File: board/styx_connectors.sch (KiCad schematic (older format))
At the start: 15 parts, among them J3 Conn_01x08, J4 Styx_P4, J5 Styx_P5

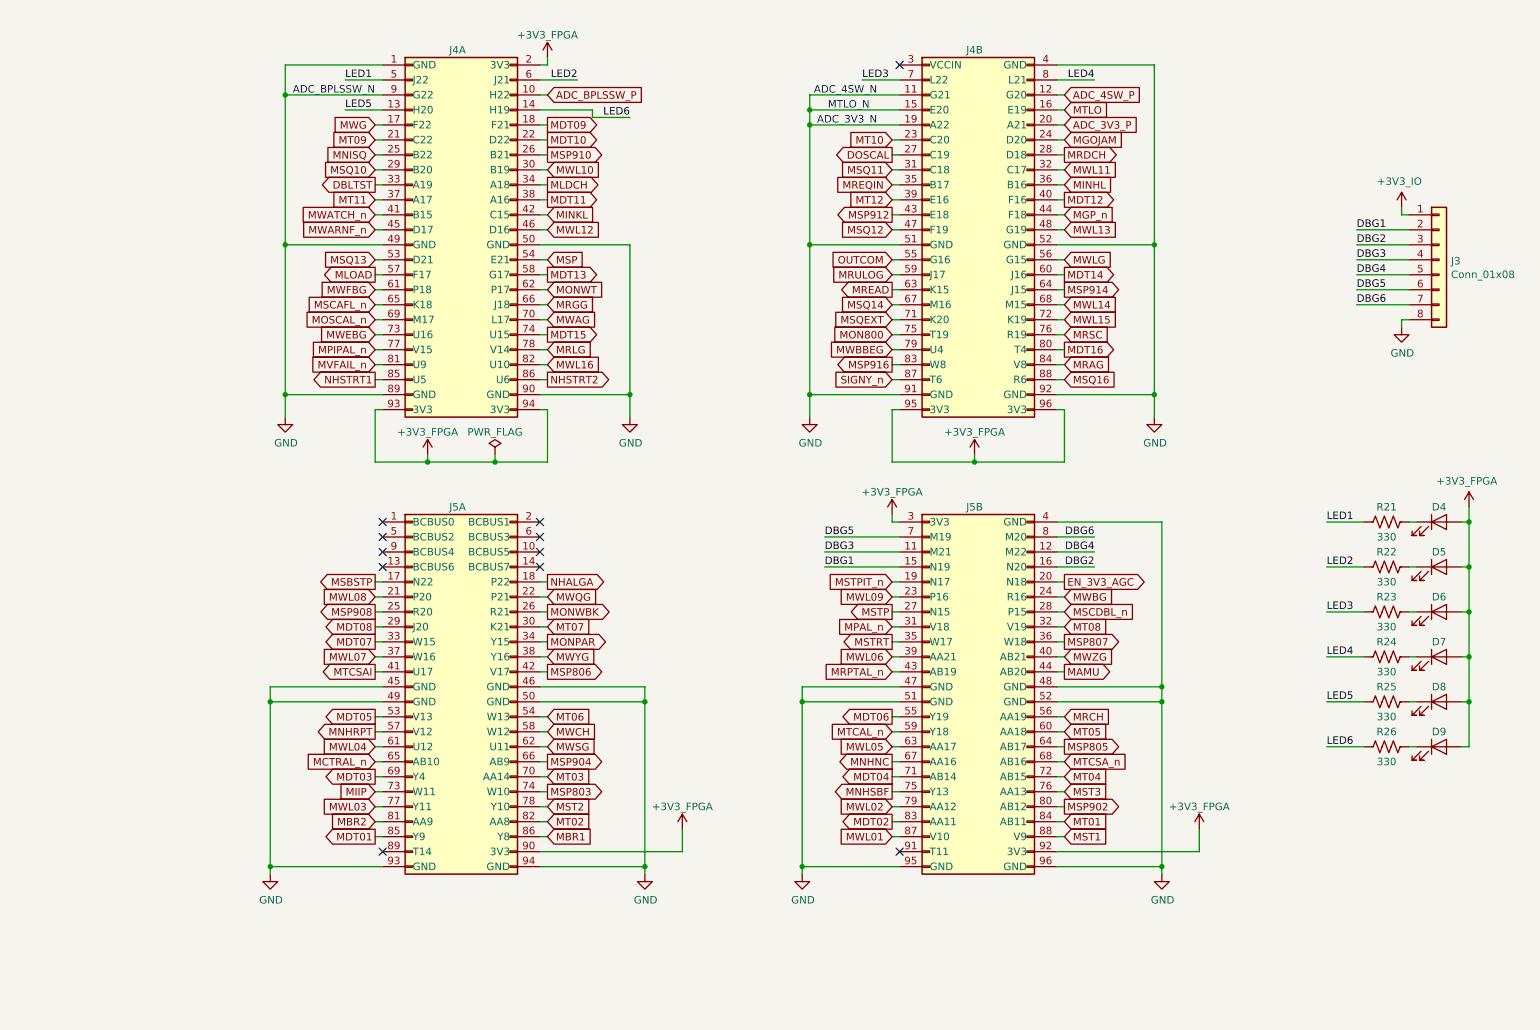
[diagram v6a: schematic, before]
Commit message: Redid the mechanical outline of the board; further development/layout
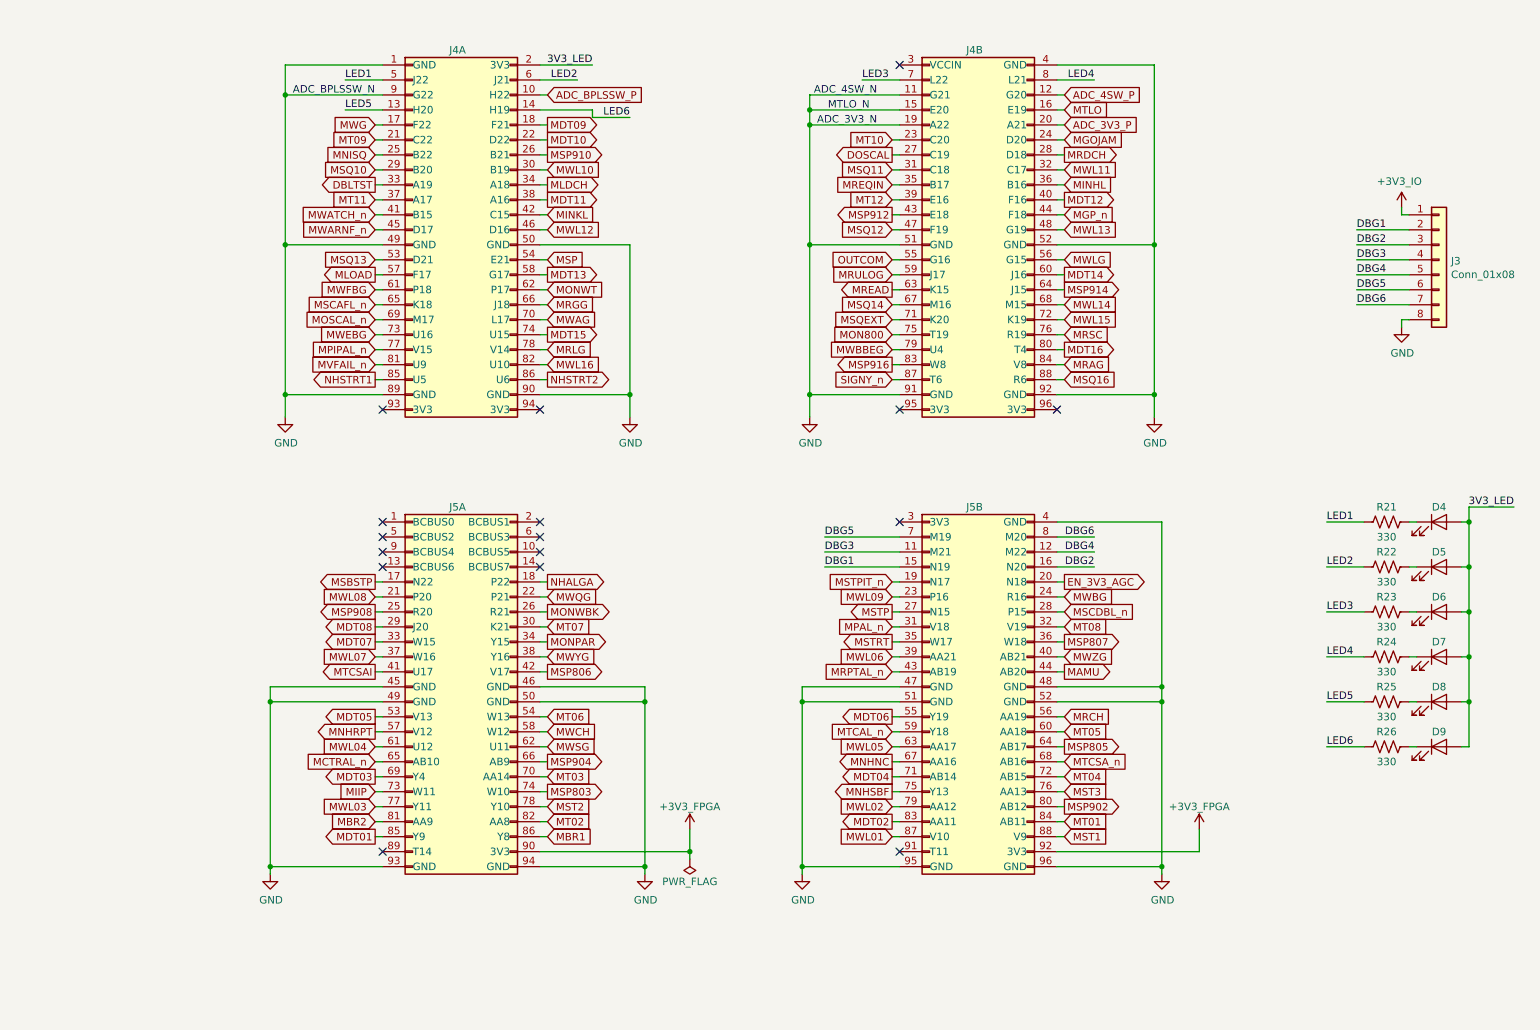
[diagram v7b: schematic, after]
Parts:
- J3: footprint Connector_PinHeader_2.54mm:PinHeader_2x04_P2.54mm_Vertical -> Connector_PinSocket_2.54mm:PinSocket_2x04_P2.54mm_Vertical
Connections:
- net +3V3_FPGA: no longer D4.2 (A), D5.2 (A), D6.2 (A), D7.2 (A), D8.2 (A), D9.2 (A), J4.2 (3V3), J4.93 (3V3), J4.94 (3V3), J4.95 (3V3), J4.96 (3V3), J5.3 (3V3)
- new net 3V3_LED: D4.2 (A), D5.2 (A), D6.2 (A), D7.2 (A), D8.2 (A), D9.2 (A), J4.2 (3V3)
- no-connect marks 11 -> 16
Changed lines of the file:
@@
 NoConn ~ 6150 850
 Wire Wire Line
-	3750 850  3800 850
-Wire Wire Line
-	3800 850  3800 800
-$Comp
-L agc_monitor:+3V3_FPGA #PWR0144
-U 1 1 5E187E74
-P 3800 800
-F 0 "#PWR0144" H 3800 650 50  0001 C CNN
-F 1 "+3V3_FPGA" H 3800 950 50  0000 C CNN
-F 2 "" H 3800 800 50  0001 C CNN
-F 3 "" H 3800 800 50  0001 C CNN
-	1    3800 800
-	1    0    0    -1
-$EndComp
+	3750 850  4100 850
 Text GLabel 2650 1450 0    50   Input ~ 0
 MNISQ
@@
 Wire Wire Line
 	3800 2450 3750 2450
-Wire Wire Line
-	2700 3150 2650 3150
-Wire Wire Line
-	2650 3150 2650 3500
-Wire Wire Line
-	2650 3500 3000 3500
-Wire Wire Line
-	3800 3500 3800 3150
-Wire Wire Line
-	3800 3150 3750 3150
-$Comp
-L agc_monitor:+3V3_FPGA #PWR0146
-U 1 1 5E198095
-P 3000 3450
-F 0 "#PWR0146" H 3000 3300 50  0001 C CNN
-F 1 "+3V3_FPGA" H 3000 3600 50  0000 C CNN
-F 2 "" H 3000 3450 50  0001 C CNN
-F 3 "" H 3000 3450 50  0001 C CNN
-	1    3000 3450
-	1    0    0    -1
-$EndComp
-Wire Wire Line
-	3000 3500 3000 3450
-Connection ~ 3000 3500
-Wire Wire Line
-	3000 3500 3450 3500
 Text GLabel 6100 1650 0    50   Input ~ 0
 MREQIN
@@
 	1    0    0    -1
 $EndComp
-Wire Wire Line
-	6100 3150 6100 3500
-Wire Wire Line
-	6100 3500 6650 3500
-Wire Wire Line
-	7250 3500 7250 3150
-$Comp
-L agc_monitor:+3V3_FPGA #PWR0148
-U 1 1 5E1A97CC
-P 6650 3450
-F 0 "#PWR0148" H 6650 3300 50  0001 C CNN
-F 1 "+3V3_FPGA" H 6650 3600 50  0000 C CNN
-F 2 "" H 6650 3450 50  0001 C CNN
-F 3 "" H 6650 3450 50  0001 C CNN
-	1    6650 3450
-	1    0    0    -1
-$EndComp
-Wire Wire Line
-	6650 3500 6650 3450
-Connection ~ 6650 3500
-Wire Wire Line
-	6650 3500 7250 3500
-Wire Wire Line
-	6150 3150 6100 3150
-Wire Wire Line
-	7250 3150 7200 3150
 Text Notes 6000 1050 2    50   ~ 0
 ADC_4SW_N
@@
 	2650 2950 2700 2950
 Wire Wire Line
-	3750 6100 4700 6100
-Wire Wire Line
-	4700 6100 4700 5950
+	3750 6100 4750 6100
+Wire Wire Line
+	4750 6100 4750 5950
 $Comp
 L agc_monitor:+3V3_FPGA #PWR0150
 U 1 1 5E3AF74D
-P 4700 5950
-F 0 "#PWR0150" H 4700 5800 50  0001 C CNN
-F 1 "+3V3_FPGA" H 4700 6100 50  0000 C CNN
-F 2 "" H 4700 5950 50  0001 C CNN
-F 3 "" H 4700 5950 50  0001 C CNN
-	1    4700 5950
+P 4750 5950
+F 0 "#PWR0150" H 4750 5800 50  0001 C CNN
+F 1 "+3V3_FPGA" H 4750 6100 50  0000 C CNN
+F 2 "" H 4750 5950 50  0001 C CNN
+F 3 "" H 4750 5950 50  0001 C CNN
+	1    4750 5950
 	1    0    0    -1
 $EndComp
@@
 	7900 6250 7900 6200
 Connection ~ 7900 6200
-Wire Wire Line
-	6150 3900 6100 3900
-Wire Wire Line
-	6100 3900 6100 3850
-$Comp
-L agc_monitor:+3V3_FPGA #PWR0155
-U 1 1 5E412C0B
-P 6100 3850
-F 0 "#PWR0155" H 6100 3700 50  0001 C CNN
-F 1 "+3V3_FPGA" H 6100 4000 50  0000 C CNN
-F 2 "" H 6100 3850 50  0001 C CNN
-F 3 "" H 6100 3850 50  0001 C CNN
-	1    6100 3850
-	1    0    0    -1
-$EndComp
 Text GLabel 6100 2650 0    50   Input ~ 0
 MON800
@@
 Wire Wire Line
 	9500 2550 9550 2550
-$Comp
-L agc_monitor:+3V3_IO #PWR0158
-U 1 1 5E993DA6
-P 9500 1800
-F 0 "#PWR0158" H 9500 1650 50  0001 C CNN
-F 1 "+3V3_IO" H 9485 1973 50  0000 C CNN
-F 2 "" H 9500 1800 50  0001 C CNN
-F 3 "" H 9500 1800 50  0001 C CNN
-	1    9500 1800
-	1    0    0    -1
-$EndComp
-Wire Wire Line
-	9500 1800 9500 1850
 Wire Wire Line
 	9500 1850 9550 1850
@@
 	9950 3900 9950 3800
 $Comp
-L agc_monitor:+3V3_FPGA #PWR0159
-U 1 1 5EA31B9C
-P 9950 3800
-F 0 "#PWR0159" H 9950 3650 50  0001 C CNN
-F 1 "+3V3_FPGA" H 9935 3973 50  0000 C CNN
-F 2 "" H 9950 3800 50  0001 C CNN
-F 3 "" H 9950 3800 50  0001 C CNN
-	1    9950 3800
-	1    0    0    -1
-$EndComp
-$Comp
 L Device:LED D5
 U 1 1 5EA444DA
@@
 L power:PWR_FLAG #FLG0102
 U 1 1 5DCB357C
-P 3450 3450
-F 0 "#FLG0102" H 3450 3525 50  0001 C CNN
-F 1 "PWR_FLAG" H 3450 3600 50  0000 C CNN
-F 2 "" H 3450 3450 50  0001 C CNN
-F 3 "~" H 3450 3450 50  0001 C CNN
-	1    3450 3450
-	1    0    0    -1
-$EndComp
-Wire Wire Line
-	3450 3450 3450 3500
-Connection ~ 3450 3500
-Wire Wire Line
-	3450 3500 3800 3500
+P 4750 6150
+F 0 "#FLG0102" H 4750 6225 50  0001 C CNN
+F 1 "PWR_FLAG" H 4750 6300 50  0000 C CNN
+F 2 "" H 4750 6150 50  0001 C CNN
+F 3 "~" H 4750 6150 50  0001 C CNN
+	1    4750 6150
+	-1   0    0    1
+$EndComp
 Text GLabel 3800 2950 2    50   Output ~ 0
 NHSTRT2
@@
 F 0 "J3" H 9830 2142 50  0000 L CNN
 F 1 "Conn_01x08" H 9830 2051 50  0000 L CNN
-F 2 "Connector_PinHeader_2.54mm:PinHeader_2x04_P2.54mm_Vertical" H 9750 2150 50  0001 C CNN
+F 2 "Connector_PinSocket_2.54mm:PinSocket_2x04_P2.54mm_Vertical" H 9750 2150 50  0001 C CNN
 F 3 "~" H 9750 2150 50  0001 C CNN
 	1    9750 2150
@@
 Text Label 7450 4000 2    50   ~ 0
 DBG6
+NoConn ~ 3750 3150
+NoConn ~ 2700 3150
+NoConn ~ 7200 3150
+NoConn ~ 6150 3150
+Wire Wire Line
+	9500 1800 9500 1850
+$Comp
+L agc_monitor:+3V3_IO #PWR0158
+U 1 1 5E993DA6
+P 9500 1800
+F 0 "#PWR0158" H 9500 1650 50  0001 C CNN
+F 1 "+3V3_IO" H 9485 1973 50  0000 C CNN
+F 2 "" H 9500 1800 50  0001 C CNN
+F 3 "" H 9500 1800 50  0001 C CNN
+	1    9500 1800
+	1    0    0    -1
+$EndComp
+NoConn ~ 6150 3900
+Text Label 4100 850  2    50   ~ 0
+3V3_LED
+Wire Wire Line
+	10250 3800 9950 3800
+Text Label 10250 3800 2    50   ~ 0
+3V3_LED
+Wire Wire Line
+	4750 6150 4750 6100
+Connection ~ 4750 6100
 $EndSCHEMATC

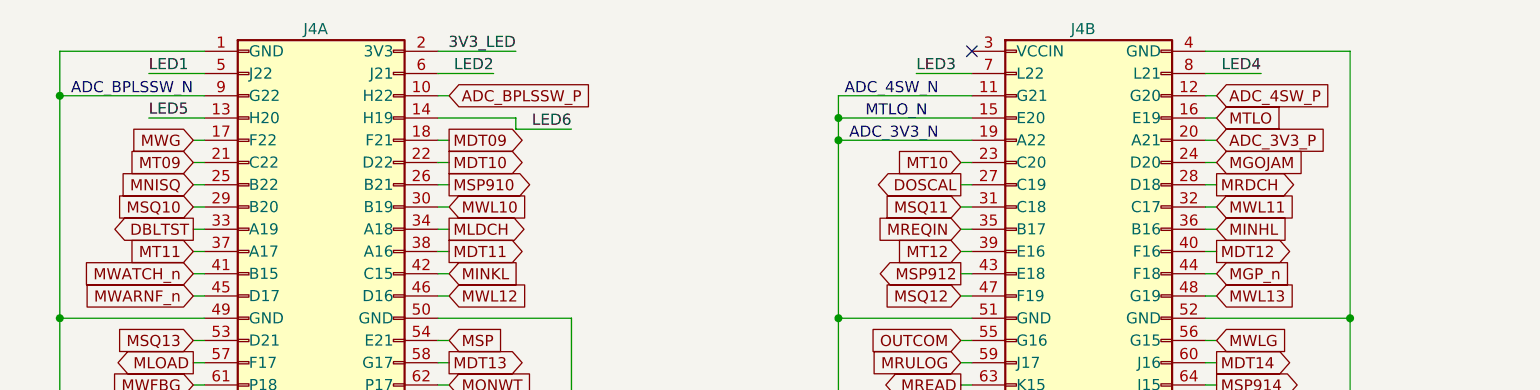
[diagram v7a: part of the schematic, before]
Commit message: Board: completed initial layout
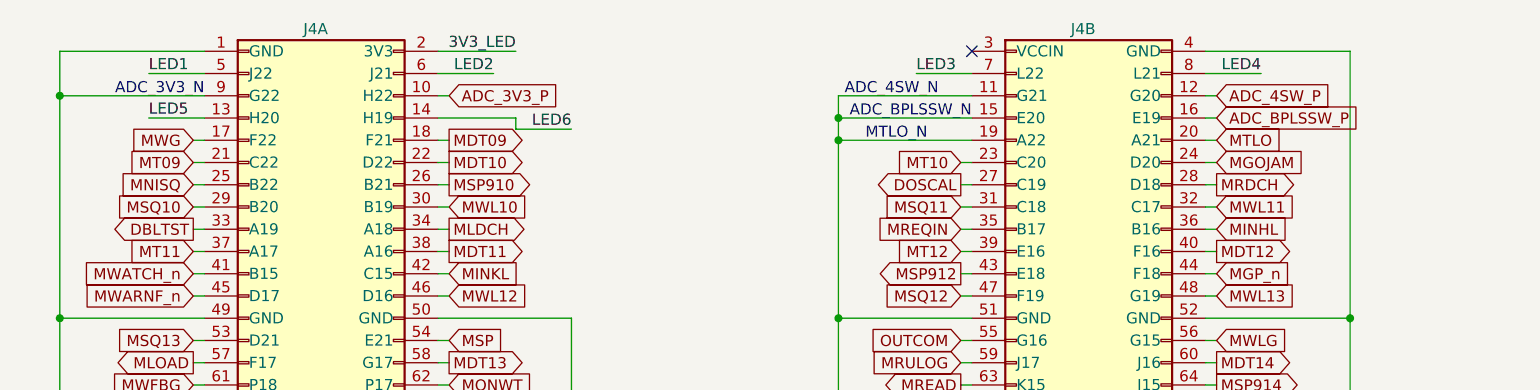
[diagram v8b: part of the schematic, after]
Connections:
- net ADC_3V3_P: now also J4.10 (H22); no longer J4.20 (A21)
- net ADC_BPLSSW_P: now also J4.16 (E19); no longer J4.10 (H22)
- net MTLO: now also J4.20 (A21); no longer J4.16 (E19)
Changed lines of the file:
@@
 	2700 1050 2050 1050
 Connection ~ 2050 1050
-Text Notes 2100 1050 0    50   ~ 0
+Text Notes 5600 1150 0    50   ~ 0
 ADC_BPLSSW_N
 Text GLabel 3800 5300 2    50   Input ~ 0
@@
 Wire Wire Line
 	2650 1450 2700 1450
-Text GLabel 3800 1050 2    50   Input ~ 0
+Text GLabel 7250 1150 2    50   Input ~ 0
 ADC_BPLSSW_P
 Wire Wire Line
-	3800 1050 3750 1050
+	7250 1150 7200 1150
 Text GLabel 7250 5200 2    50   Input ~ 0
 MRCH
@@
 Wire Wire Line
 	5550 1150 5550 1250
-Text Notes 5950 1150 2    50   ~ 0
+Text Notes 5950 1250 2    50   ~ 0
 MTLO_N
 Wire Wire Line
 	6150 1250 5550 1250
-Text Notes 6000 1250 2    50   ~ 0
+Text Notes 2700 1050 2    50   ~ 0
 ADC_3V3_N
-Text GLabel 7250 1250 2    50   Input ~ 0
+Text GLabel 3800 1050 2    50   Input ~ 0
 ADC_3V3_P
 Wire Wire Line
-	7250 1250 7200 1250
+	3800 1050 3750 1050
 Text GLabel 2650 5800 0    50   Input ~ 0
 MWL03
@@
 Wire Wire Line
 	7250 1050 7200 1050
-Text GLabel 7250 1150 2    50   Input ~ 0
+Text GLabel 7250 1250 2    50   Input ~ 0
 MTLO
 Wire Wire Line
-	7250 1150 7200 1150
+	7250 1250 7200 1250
 Text GLabel 2650 1850 0    50   Input ~ 0
 MWATCH_n
